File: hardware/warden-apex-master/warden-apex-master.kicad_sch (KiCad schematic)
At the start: 84 parts, among them IC1 SIM7080G, IC2 BQ24650RVAR, IC3 TPS63070RNMR, IC4 MAX98357AETE+T, J1 U.FL-R-SMT-1, J2 U.FL-R-SMT-1, J3 61300211121, J4 Expansion_Header, J5 Qwiic, Q1 DMG9926UDM, Q2 AO3401A, Q3 2N7002, U1 113991115, U2 Ai-Thinker-Ra-01, U3 M138 Modem, U4 MCP23017_SO, U5 SRV05-4-P-T7, U6 SC16IS740, X1 14.7456MHz

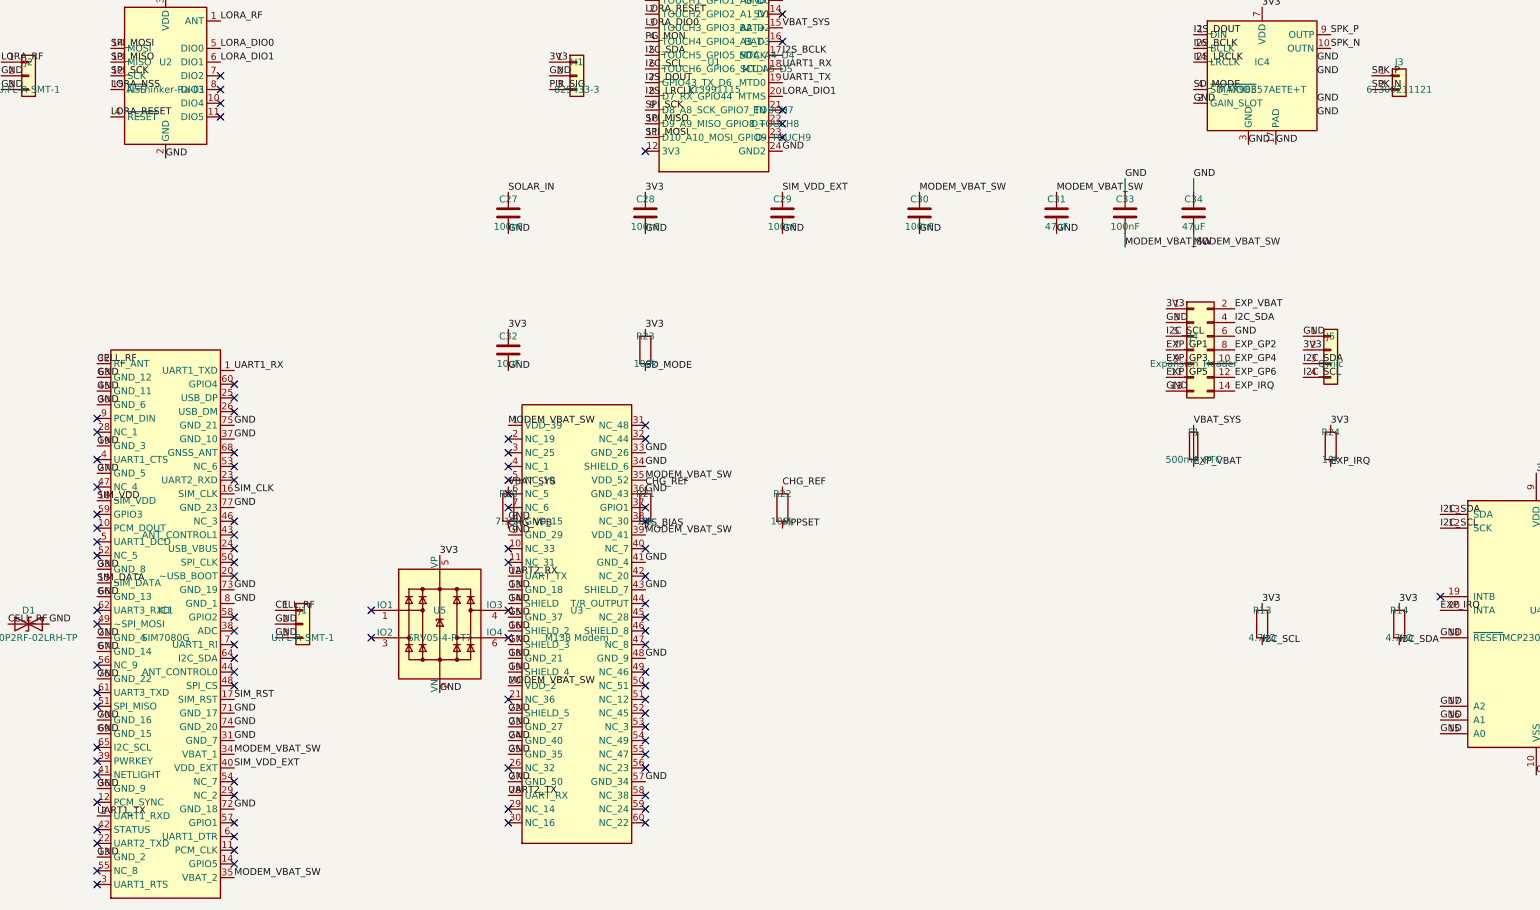
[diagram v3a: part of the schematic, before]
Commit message: Update warden-apex design to Phase 24 live state. Enhanced README.md to clarify current design status, noting that the snapshot is not yet production-ready. Adjusted BOM files to include additional resistors and capacitors, and updated component placements. Revised Gerber files with new timestamps and ensured consistency across documentation. Addressed DRC issues with 10 violations and 5 unconnected items, indicating further cleanup is required before production submission.
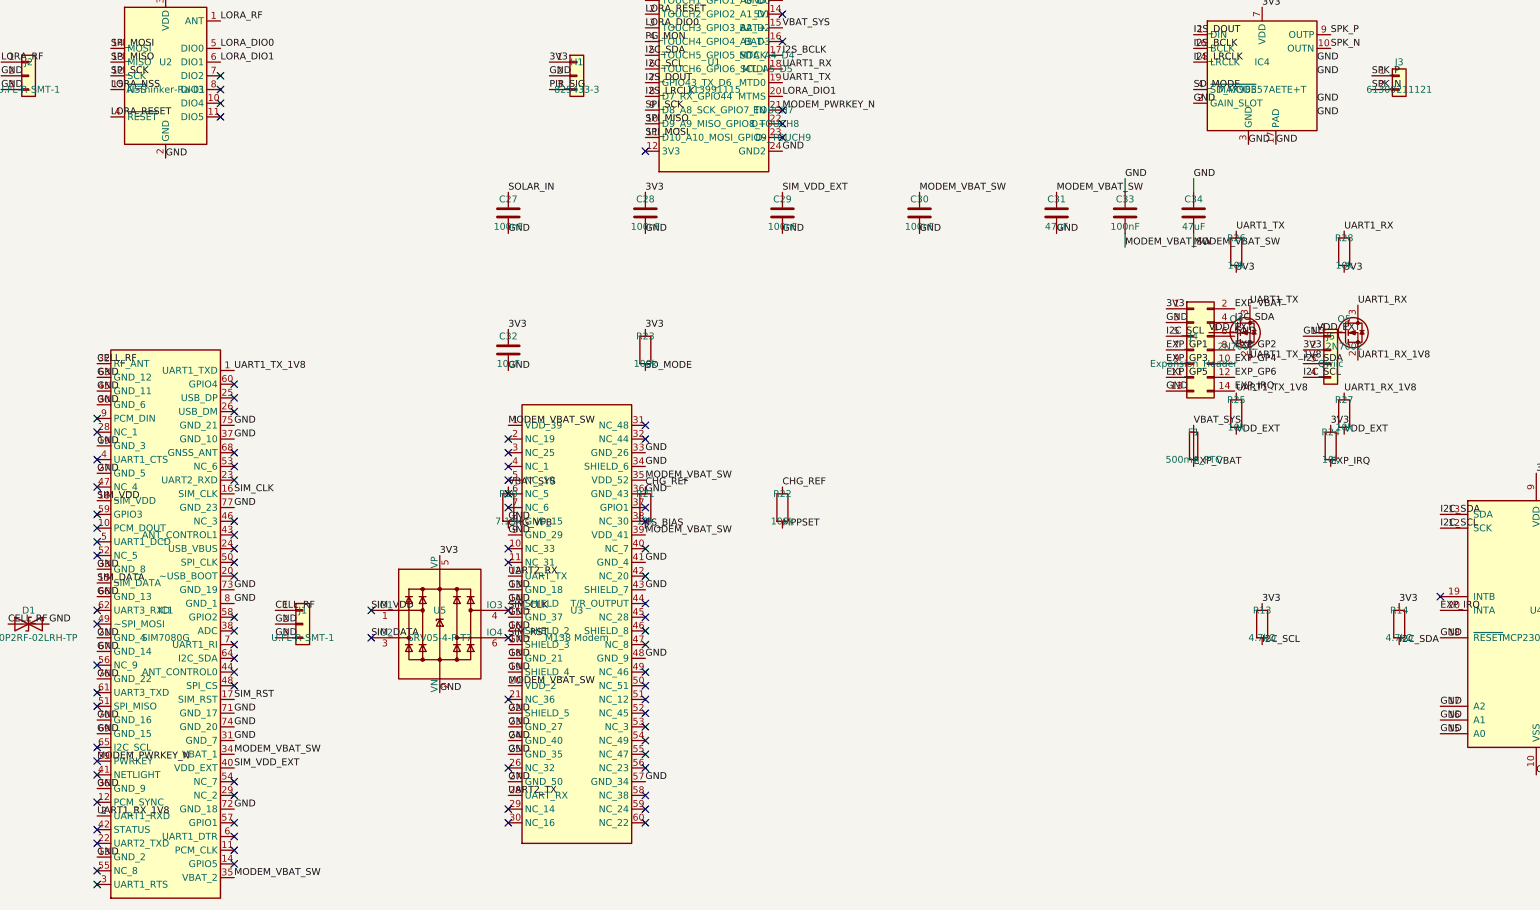
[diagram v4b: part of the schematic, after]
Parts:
- added Q4, Q5: 2N7002, Package_TO_SOT_SMD:SOT-23, symbol Transistor_FET:2N7002
- added R25, R26, R27, R28: 10k, Resistor_SMD:R_0805_2012Metric, symbol Device:R
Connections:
- net 3V3: now also R26.2, R28.2
- net SIM_CLK: now also U5.4 (IO3)
- net SIM_DATA: now also U5.3 (IO2)
- net SIM_RST: now also U5.6 (IO4)
- net SIM_VDD: now also U5.1 (IO1)
- net UART1_RX: now also Q5.3 (D), R28.1; no longer IC1.1 (UART1_TXD)
- net UART1_TX: now also Q4.3 (D), R26.1; no longer IC1.2 (UART1_RXD)
- net MODEM_PWRKEY_N: now reaches IC1.39 (PWRKEY)
- net MODEM_PWRKEY_N: now also U1.21 (EN)
- new net UART1_RX_1V8: IC1.2 (UART1_RXD), Q5.2 (S), R27.1
- new net UART1_TX_1V8: IC1.1 (UART1_TXD), Q4.2 (S), R25.1
- new net VDD_EXT: Q4.1 (G), Q5.1 (G), R25.2, R27.2

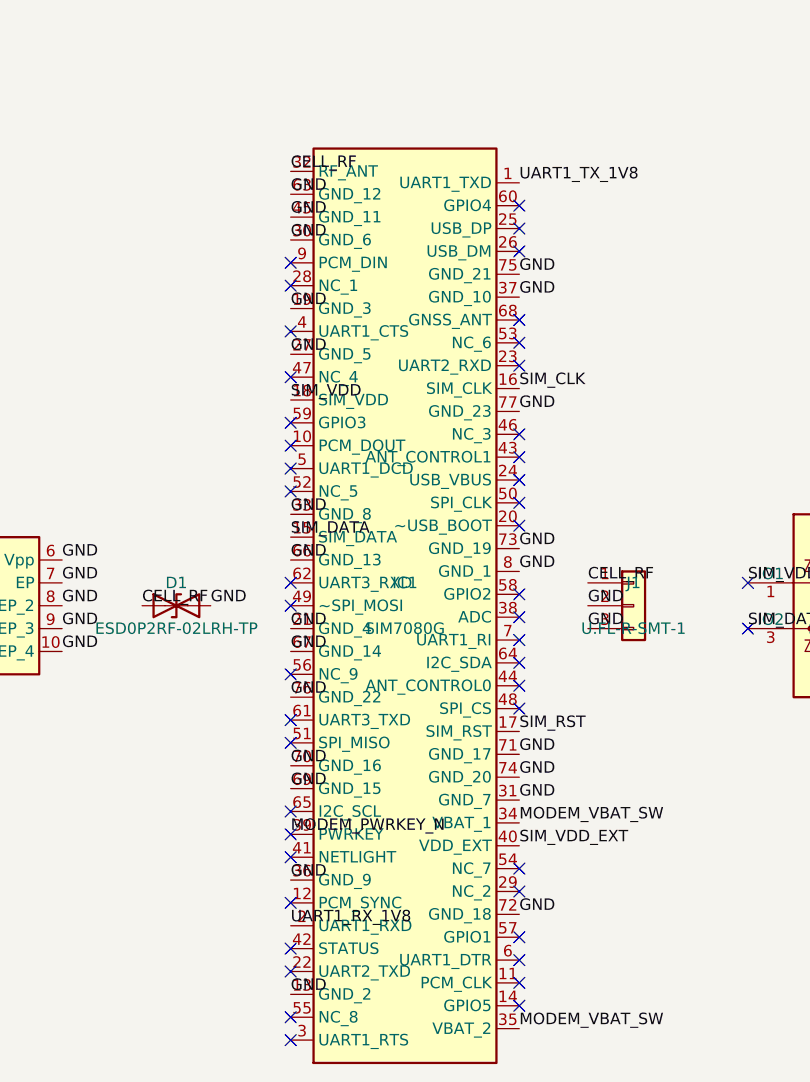
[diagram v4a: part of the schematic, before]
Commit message: Remove obsolete ERC report file and update README.md to reflect the current post-repair release snapshot. Adjusted DRC results to indicate zero violations and unconnected items, confirming readiness for fabrication. Updated Gerber files with new timestamps for consistency across documentation.
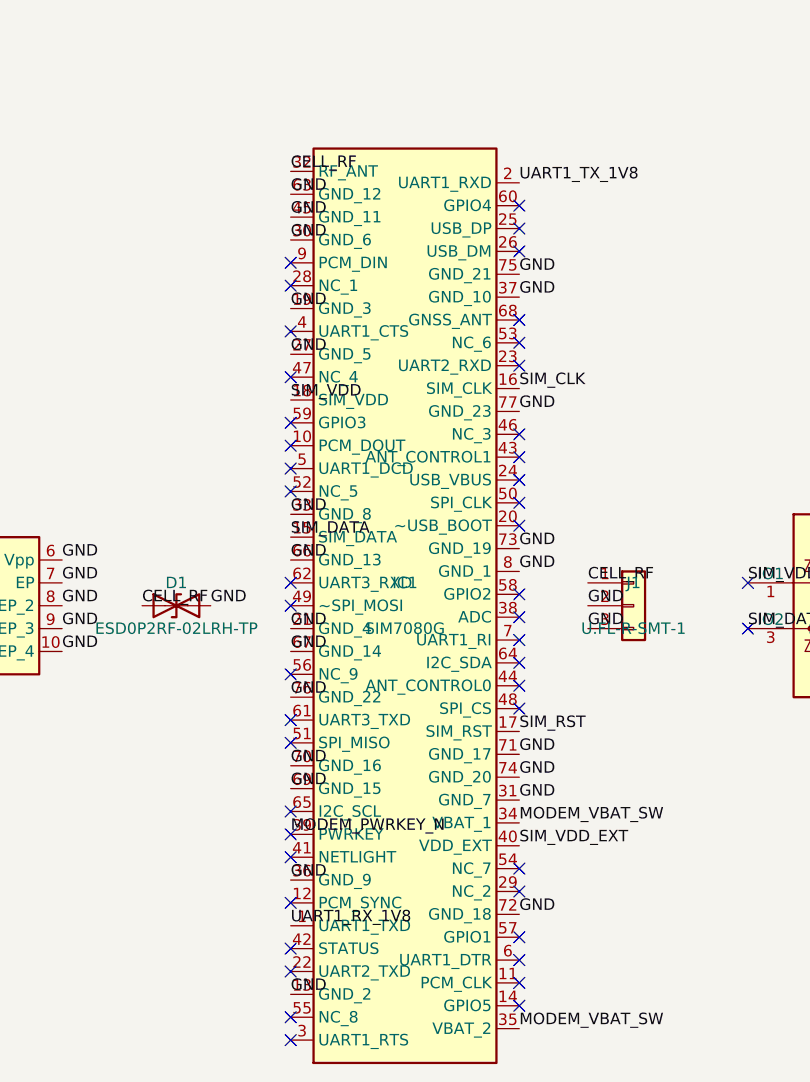
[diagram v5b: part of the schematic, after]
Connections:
- net UART1_RX_1V8: now also IC1.1 (UART1_TXD); no longer IC1.2 (UART1_RXD)
- net UART1_TX_1V8: now also IC1.2 (UART1_RXD); no longer IC1.1 (UART1_TXD)

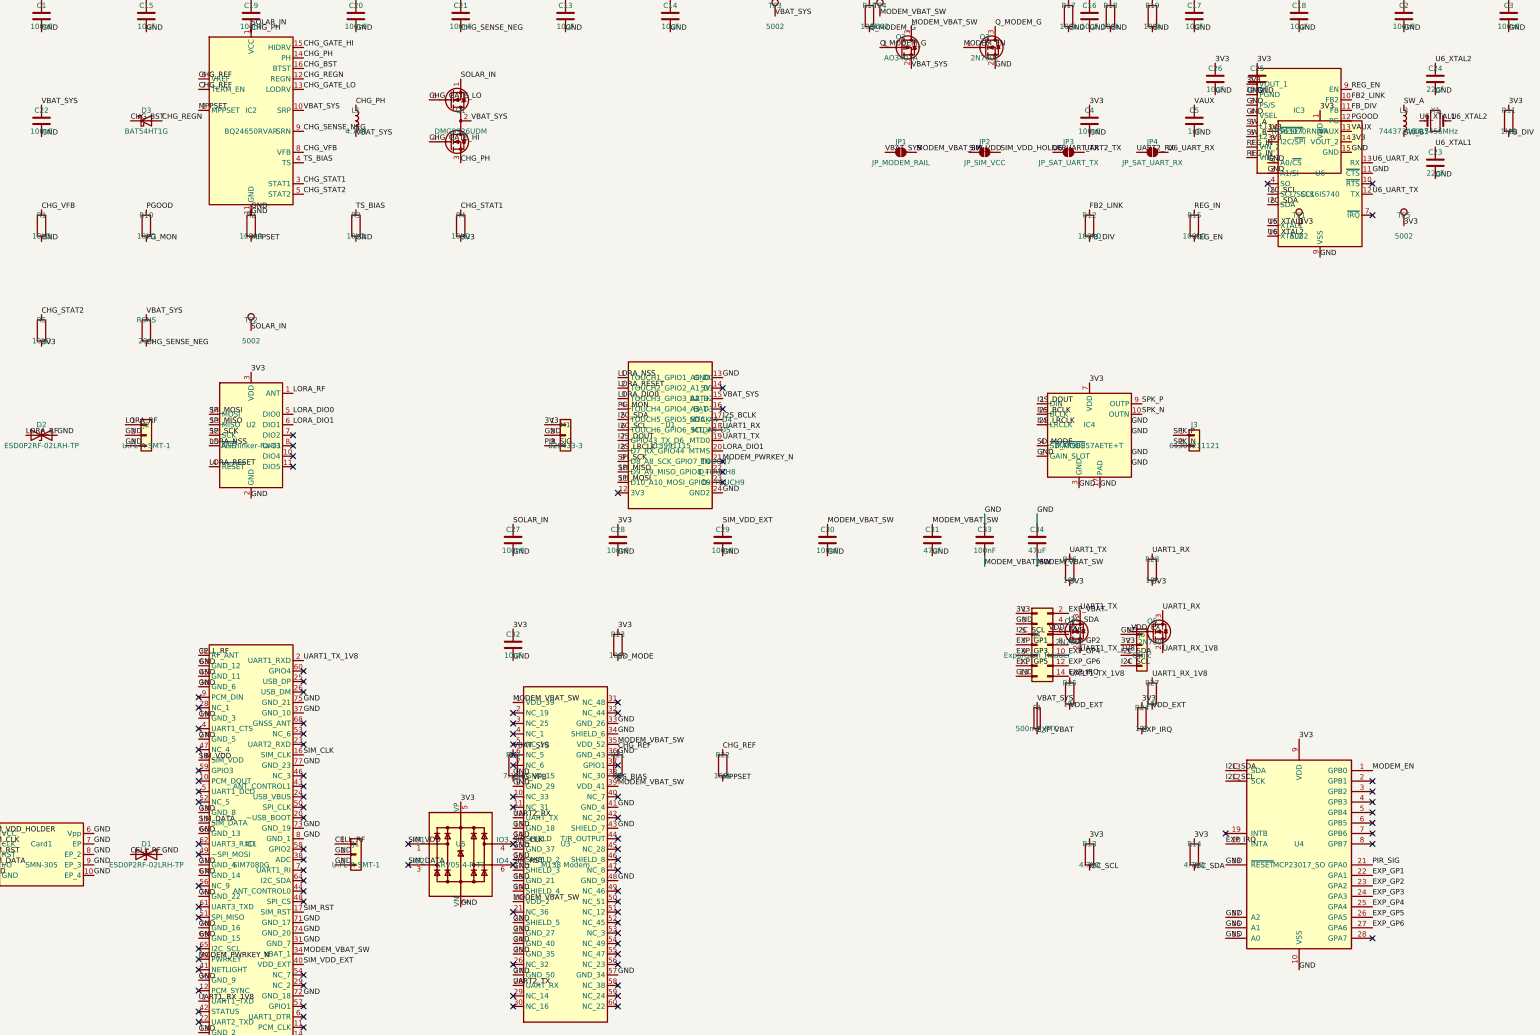
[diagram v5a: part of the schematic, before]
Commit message: Refactor warden-custom symbol by updating footprint reference and renaming pins for clarity. Adjusted pin names to better reflect their functions, enhancing overall readability and usability of the schematic. Cleaned up whitespace in PCB files for consistency.
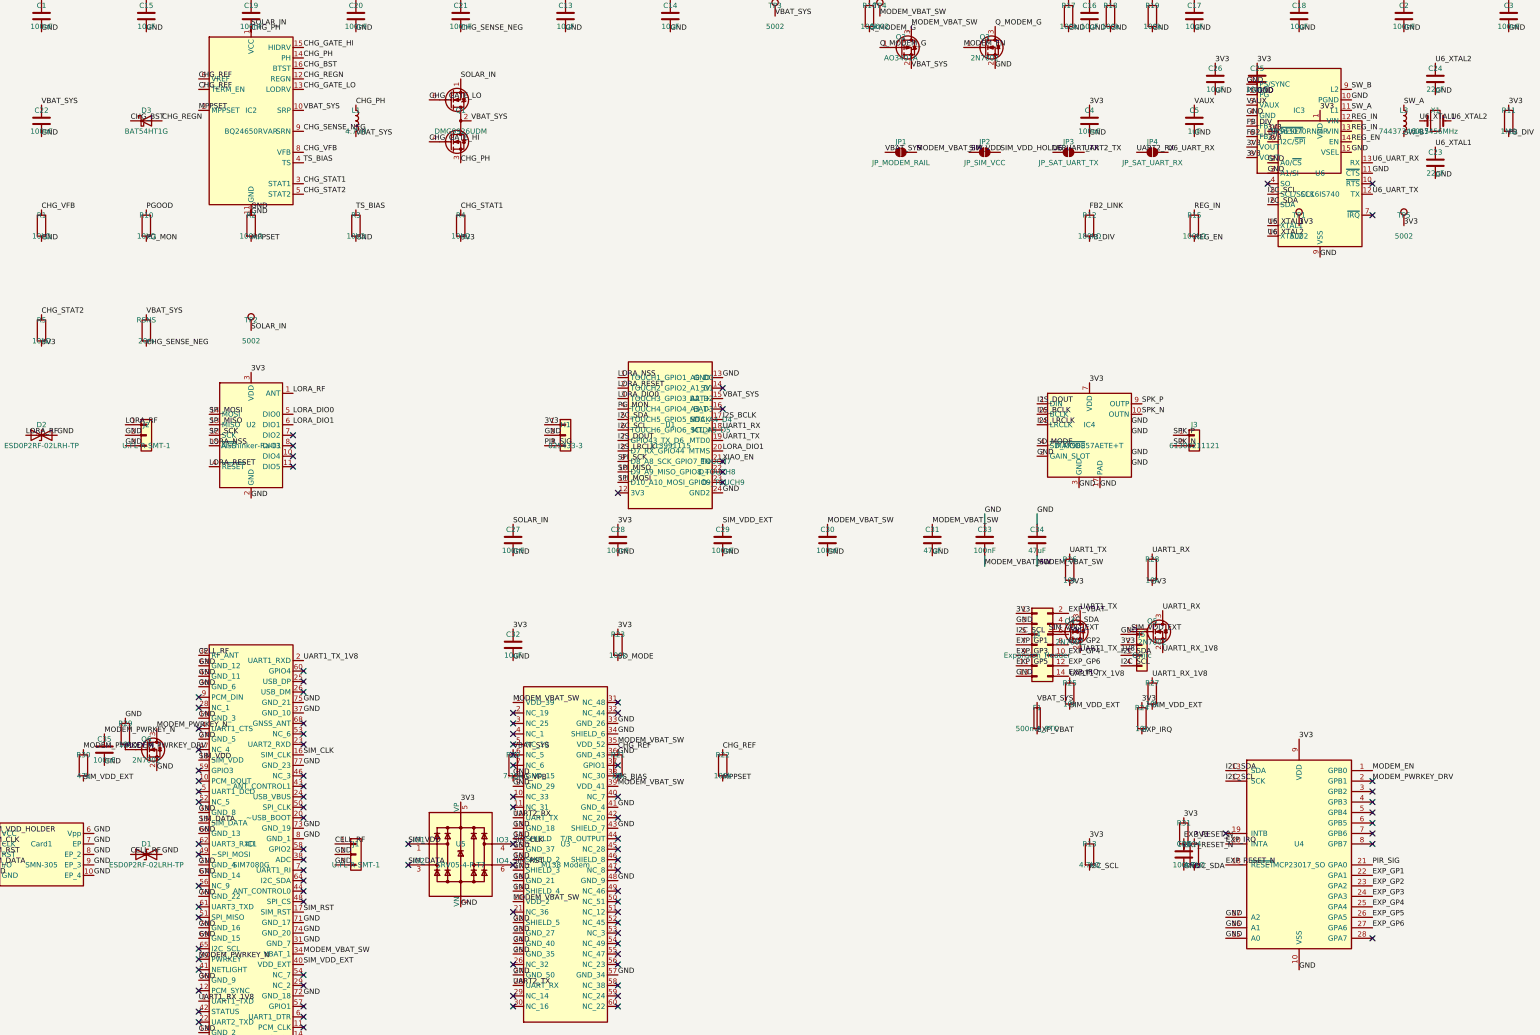
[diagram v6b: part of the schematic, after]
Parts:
- added C35, C36: 100nF, Capacitor_SMD:C_0805_2012Metric, symbol Device:C
- added Q6: 2N7002, Package_TO_SOT_SMD:SOT-23, symbol Transistor_FET:2N7002
- added R29, R31: 10k, Resistor_SMD:R_0805_2012Metric, symbol Device:R
- added R30: 47k, Resistor_SMD:R_0805_2012Metric, symbol Device:R
- IC3: footprint warden_custom:QFN-15-1EP_3x4mm_P0.5mm_EP1.45x2.45mm -> warden_custom:TPS63070_RNM0015A
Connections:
- net VDD_EXT is gone; now on net SIM_VDD_EXT: Q4.1 (G), Q5.1 (G), R25.2, R27.2
- net 3V3: now also IC3.7 (VOUT), IC3.8 (VOUT), R31.1; no longer IC3.1 (VOUT_1), IC3.14 (VOUT_2)
- net FB2_LINK: now also IC3.6 (FB2); no longer IC3.10 (FB2)
- net FB_DIV: now also IC3.5 (FB); no longer IC3.11 (FB)
- net GND: now also IC3.1 (PS/SYNC), IC3.10 (PGND), C35.2, C36.2, Q6.2 (S), R29.1; no longer IC3.2 (PGND), IC3.3 (PS/S), U4.18 (~{RESET})
- net MODEM_PWRKEY_N: now also C35.1, Q6.3 (D), R30.1; no longer U1.21 (EN)
- net PGOOD: now also IC3.2 (PG); no longer IC3.12 (PG)
- net REG_EN: now also IC3.14 (EN); no longer IC3.9 (EN)
- net REG_IN: now also IC3.12 (VIN), IC3.13 (VIN); no longer IC3.7 (VIN_2), IC3.8 (VIN_1)
- net SIM_VDD_EXT: now also R30.2
- net SW_A: now also IC3.11 (L1); no longer IC3.5 (L1)
- net SW_B: now also IC3.9 (L2); no longer IC3.6 (L2)
- net VAUX: now also IC3.3 (VAUX); no longer IC3.13 (VAUX)
- net MODEM_PWRKEY_DRV: now reaches U4.2 (GPB1)
- net MODEM_PWRKEY_DRV: now also Q6.1 (G), R29.2
- new net EXP_RESET_N: C36.1, R31.2, U4.18 (~{RESET})
- new net XIAO_EN: U1.21 (EN)

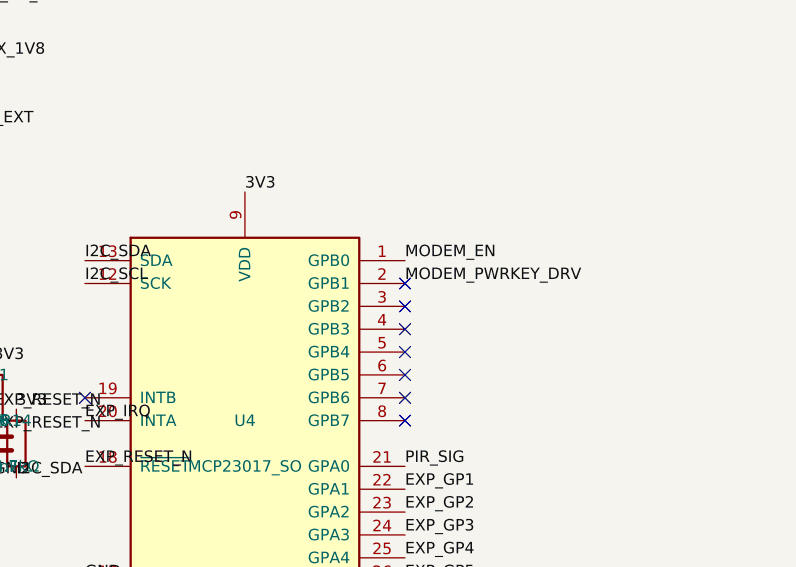
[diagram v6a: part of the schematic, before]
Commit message: Update warden-apex design with revised DRC and ERC results, reflecting current warnings and violations. Adjusted README.md to clarify design status and known caveats. Updated Gerber files with new timestamps for consistency. Renamed components in the master position file for clarity and improved organization.
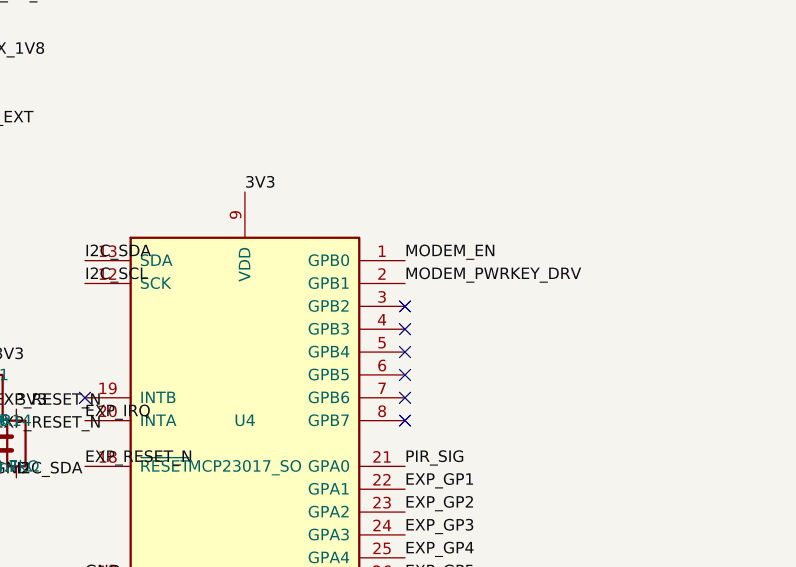
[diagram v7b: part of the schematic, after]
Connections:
- no-connect marks 103 -> 102
